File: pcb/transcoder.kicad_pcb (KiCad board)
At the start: 2 copper layers, 75.8 x 50 mm, 39 parts, among them J1 MD-90SM, J2 Connector_RCA_2x3_REB, M0 MountingHole_3.2mm_M3, U1 BA7230LS, U2 LM1881, U3 THS7374

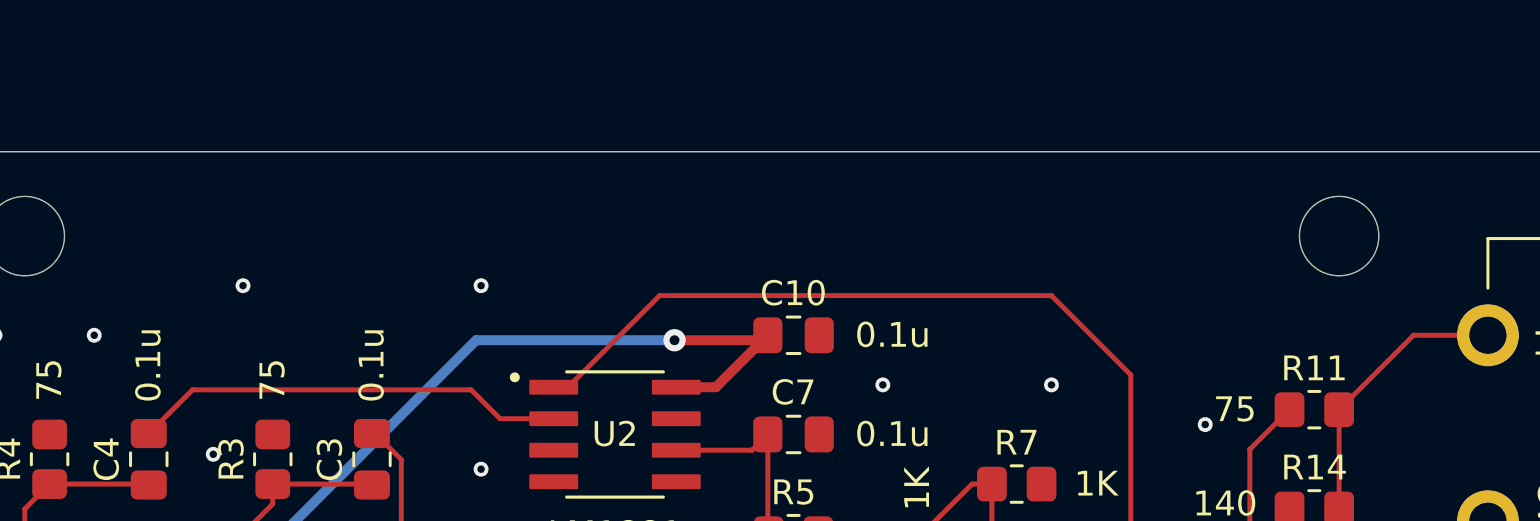
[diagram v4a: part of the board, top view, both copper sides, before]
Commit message: Adds silkscreens
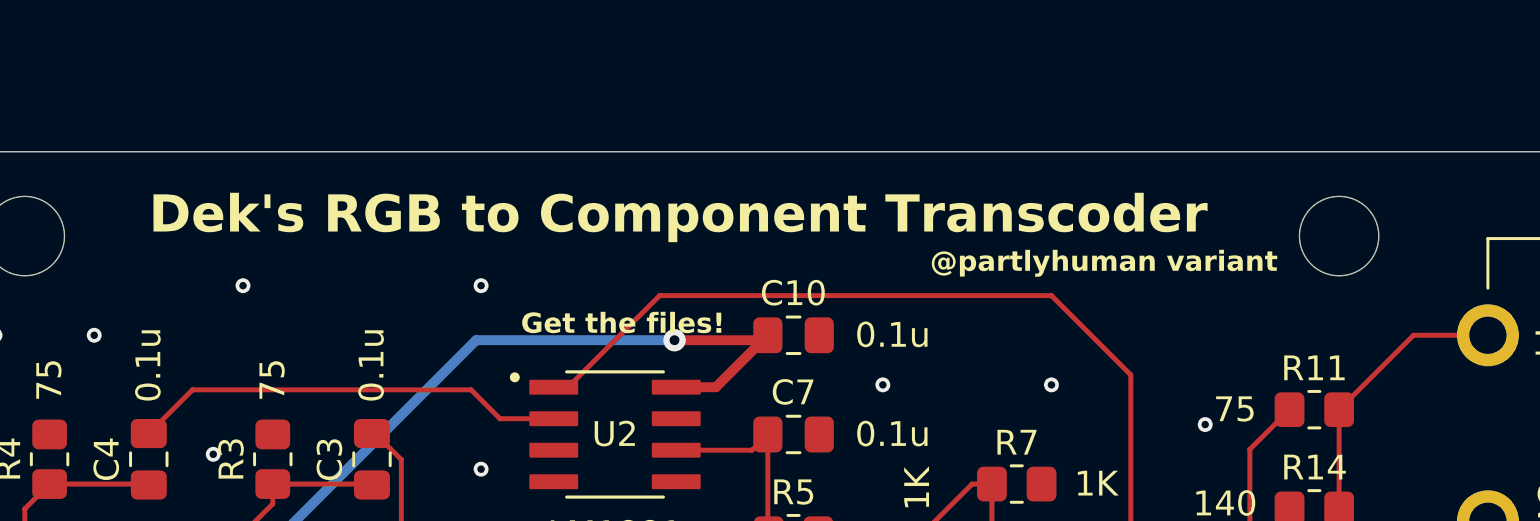
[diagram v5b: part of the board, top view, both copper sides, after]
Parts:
- added G***: LOGO, REB_Transcoder:QR2, B.Cu at (165.0, 107.0)
- added G***: LOGO, REB_Transcoder:QR1, B.Cu at (165.0, 82.0)
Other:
- board text added: "@partlyhuman variant"
- board text added: "Dek's RGB to Component Transcoder"
- board text added: "Get the files!"
- board text added: "Original by @dekkit et al"
- board text added: "This fork by @partlyhuman"

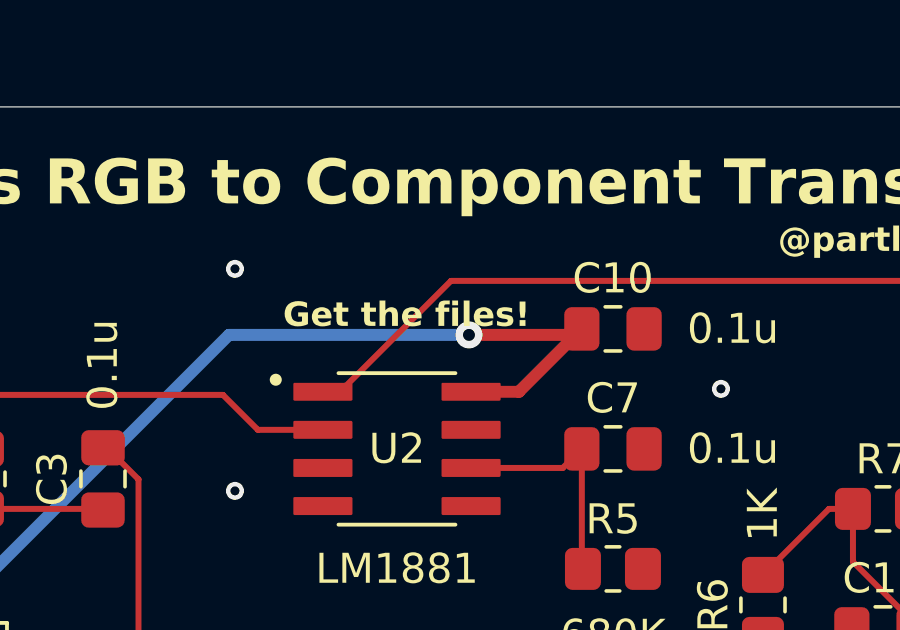
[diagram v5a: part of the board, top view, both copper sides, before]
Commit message: Removes stray text
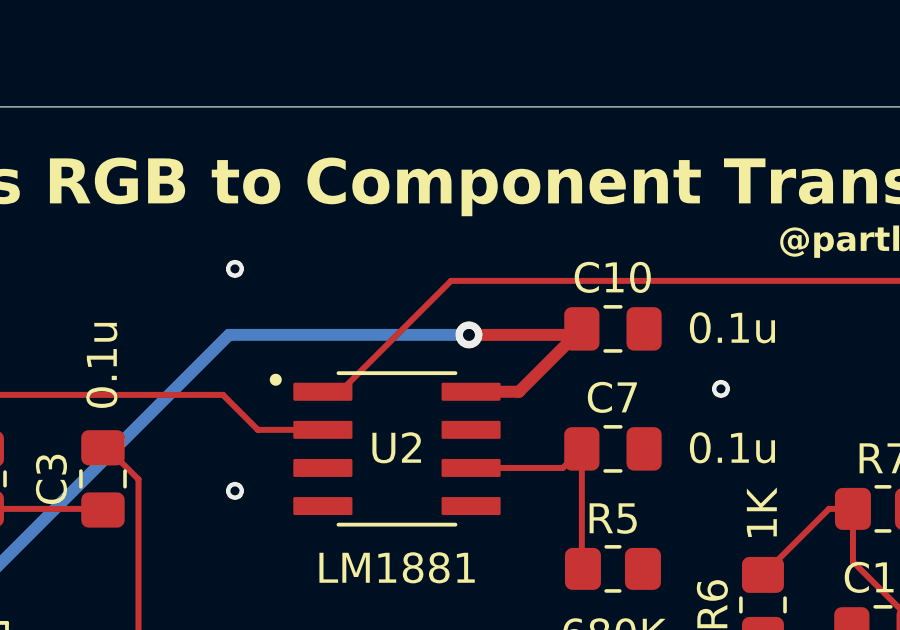
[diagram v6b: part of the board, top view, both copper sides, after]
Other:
- board text removed: "Get the files!"
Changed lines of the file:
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@@
-    (effects (font (size 0.8128 0.8128) (thickness 0.1524) bold) (justify left bottom))
-  )
-  (gr_text "Get the files!" (at 143 78) (layer "F.SilkS")
     (effects (font (size 0.8128 0.8128) (thickness 0.1524) bold) (justify left bottom))
   )
